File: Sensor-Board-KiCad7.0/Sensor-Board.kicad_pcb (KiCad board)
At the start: 2 copper layers, 61 x 22.9 mm, 128 parts, among them J1 B4B-XH-A, U1 OPA396DCKT, U10 BME680, U11 OPA396DCKT, U12 OPA396DCKT, U13 TCA9548AMRGER, U14 OPA396DCKT, U15 MMBFJ177LT1, U16 MMBFJ177LT1, U17 MMBFJ177LT1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

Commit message: Added gas cell contour and Echem sensors
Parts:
- moved U10 234.4 mm to (121.8, 95.7), turned to -90 degrees
- moved U27 148.2 mm to (131.3, 91.7)
- moved U28 143.0 mm to (138.2, 84.2), turned to -90 degrees
- moved U23 139.1 mm to (144.1, 98.9), turned to 180 degrees
- moved U6 129.5 mm to (153.8, 95.5)
- moved U29 121.8 mm to (137.1, 96.8), turned to 90 degrees
- moved U30 121.2 mm to (137.0, 106.9), turned to 90 degrees
- moved U31 118.4 mm to (138.2, 94.3), turned to -90 degrees
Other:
- board size 61 x 22.9 mm -> 188.3 x 126.4 mm

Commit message: Clarified exclusion zones and started layout
Clarified the zones where we cannot place components and started adding components to layout.
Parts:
- moved U3 260.2 mm to (123.1, 130.9), turned to 90 degrees
- moved U2 260.1 mm to (123.2, 126.9), turned to 90 degrees
- moved U1 260.0 mm to (123.2, 122.5), turned to 90 degrees
- moved U26 247.0 mm to (133.5, 122.5), turned to -90 degrees
- moved R55 242.9 mm to (120.8, 124.8), turned to -90 degrees
- moved U20 242.7 mm to (133.5, 131.2), turned to -90 degrees
- moved U19 237.8 mm to (133.5, 127.0), turned to -90 degrees
- moved R56 236.3 mm to (126.5, 124.0), turned to 180 degrees
- moved R4 232.6 mm to (120.8, 131.2), turned to 90 degrees
- moved R57 231.5 mm to (129.8, 122.2), turned to 180 degrees
- moved R2 228.4 mm to (126.5, 128.2), turned to 180 degrees
- moved R5 226.7 mm to (126.6, 132.2), turned to 180 degrees
- moved C2 224.7 mm to (126.5, 130.5), turned to 180 degrees
- moved C1 224.0 mm to (126.5, 126.5), turned to 180 degrees
- moved R3 223.6 mm to (129.7, 126.5), turned to 180 degrees
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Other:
- outline, holes or cut-outs redrawn

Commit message: layout of pcb update (not final)
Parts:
- moved TP15 280.8 mm to (107.2, 111.8)
- moved TP14 279.1 mm to (109.9, 111.8)
- moved TP13 278.8 mm to (101.3, 102.1)
- moved R21 246.3 mm to (105.5, 116.7), turned to 45 degrees
- moved R22 242.4 mm to (107.8, 114.4), turned to -135 degrees
- moved TP16 239.1 mm to (156.1, 131.9)
- moved U21 239.0 mm to (142.5, 127.3), turned to 90 degrees
- moved U22 239.0 mm to (142.5, 131.4), turned to 90 degrees
- moved U14 238.8 mm to (142.5, 122.5), turned to 90 degrees
- moved C4 236.2 mm to (101.3, 105.2), turned to 90 degrees
- moved TP17 234.6 mm to (157.8, 127.0)
- moved TP18 232.6 mm to (159.4, 129.3)
- moved R67 226.2 mm to (139.2, 132.1), turned to 180 degrees
- moved U25 223.9 mm to (108.2, 106.4), turned to -90 degrees
- moved R69 223.3 mm to (139.2, 130.5), turned to 180 degrees
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
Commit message: Full preliminary layout
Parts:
- moved TP1 274.5 mm to (104.5, 79.8)
- moved TP2 273.7 mm to (104.5, 77.2)
- moved C9 235.1 mm to (101.0, 105.7), turned to 90 degrees
- moved C8 234.9 mm to (101.0, 102.6), turned to -90 degrees
- moved R20 227.1 mm to (104.5, 75.0), turned to 180 degrees
- moved R19 222.7 mm to (110.1, 80.2)
- moved R68 220.4 mm to (144.4, 132.2)
- moved R53 210.8 mm to (144.4, 128.2)
- moved R7 205.0 mm to (144.4, 124.2)
- moved R29 180.9 mm to (166.6, 113.2), turned to -45 degrees
- moved R16 133.6 mm to (101.0, 111.9), turned to -90 degrees
- moved C6 127.8 mm to (101.0, 89.0), turned to 90 degrees
- moved C5 127.7 mm to (101.0, 85.8), turned to -90 degrees
- moved C15 126.5 mm to (101.0, 82.6), turned to 90 degrees
- moved R17 124.3 mm to (110.0, 111.3), turned to 180 degrees
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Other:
- outline, holes or cut-outs redrawn

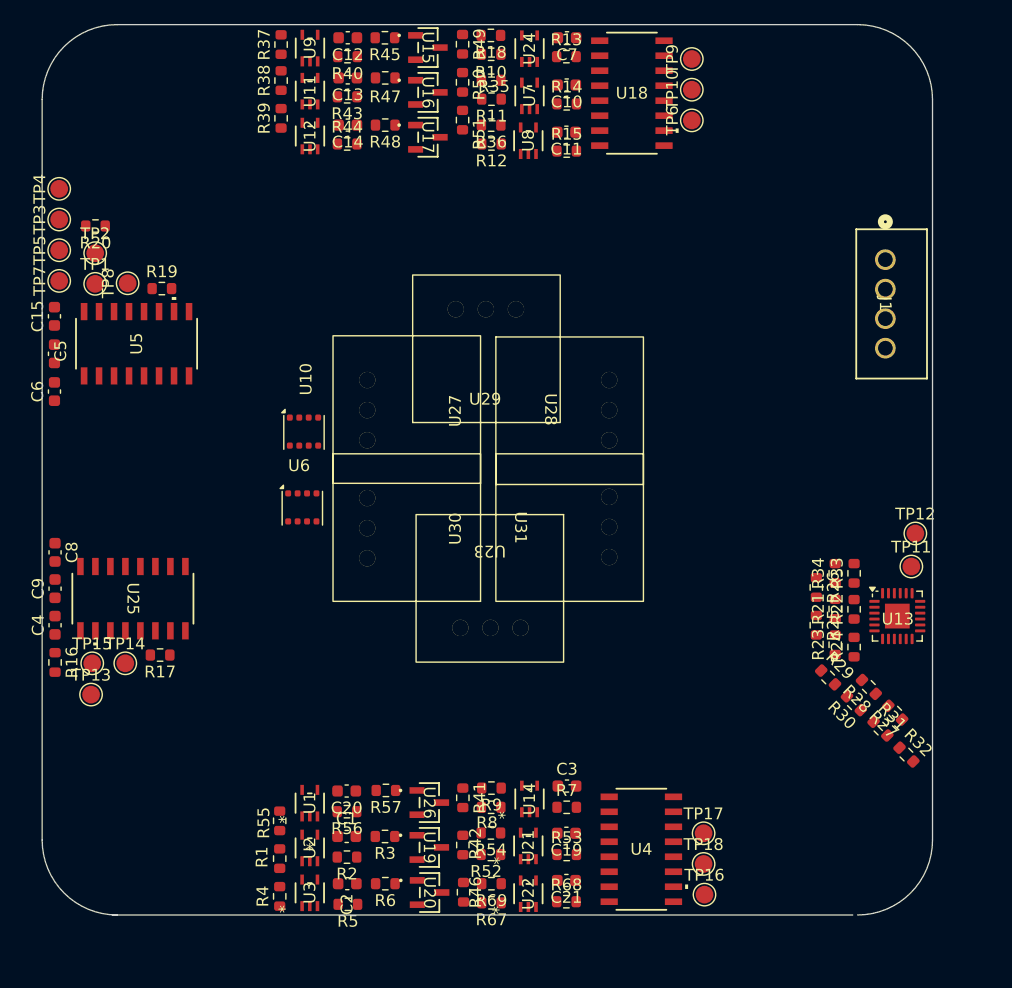
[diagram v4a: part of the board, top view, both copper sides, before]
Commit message: Fixed board dimensions
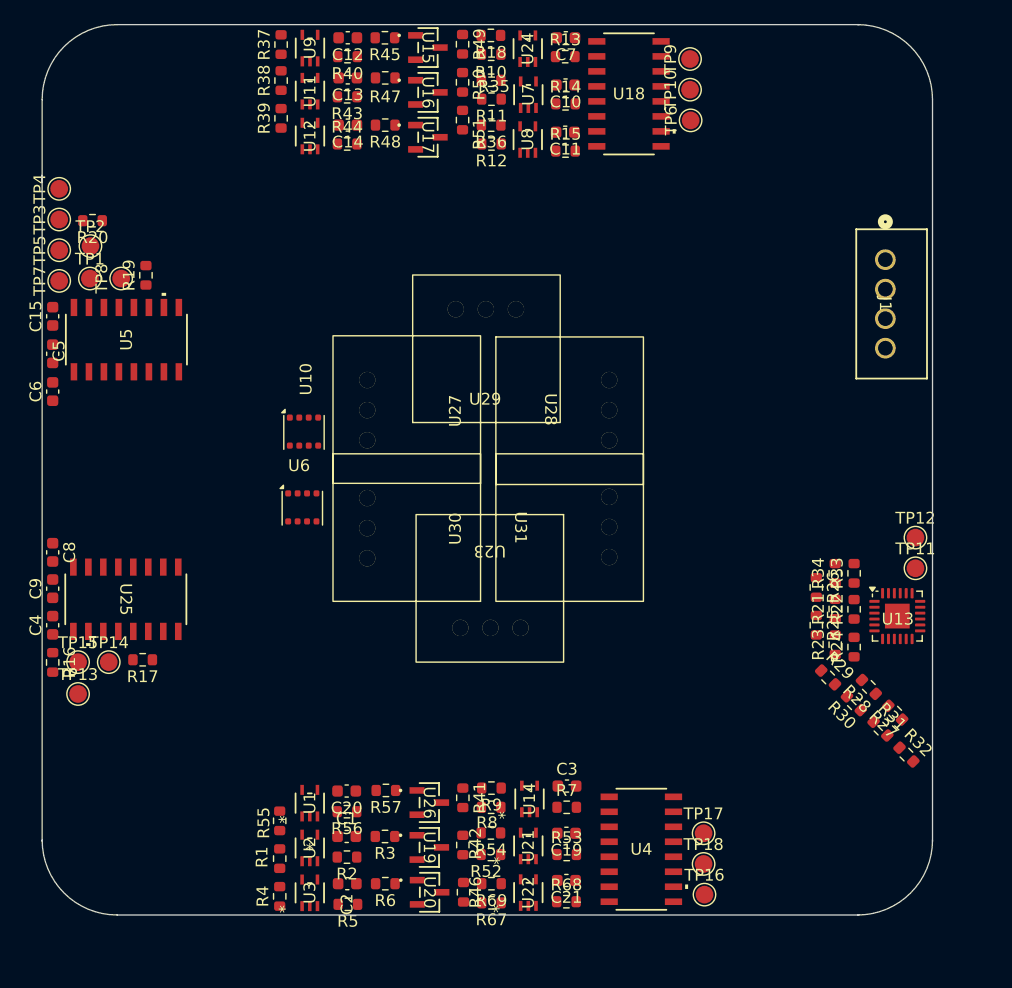
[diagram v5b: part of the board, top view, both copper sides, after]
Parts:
- moved R19 1.76 mm to (108.8, 79.1), turned to 90 degrees
- moved R17 1.53 mm to (108.5, 111.7)
- moved TP14 1.40 mm to (105.6, 111.9)
- moved TP15 1.20 mm to (103.0, 111.9)
- moved TP13 1.10 mm to (103.0, 114.6)
- moved U5 0.93 mm to (107.1, 84.6)
- moved TP2 0.72 mm to (104.0, 76.7)
- moved TP8 0.68 mm to (106.7, 79.4)
- moved TP1 0.64 mm to (104.0, 79.4)
- moved U25 0.60 mm to (107.0, 106.6)
- moved R20 0.51 mm to (104.2, 74.5)
- moved TP11 0.38 mm to (173.9, 104.0)
- moved TP12 0.35 mm to (173.9, 101.3)
- moved U18 0.26 mm to (149.7, 63.8)
- moved C4 0.20 mm to (100.8, 108.8)
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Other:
- outline, holes or cut-outs redrawn

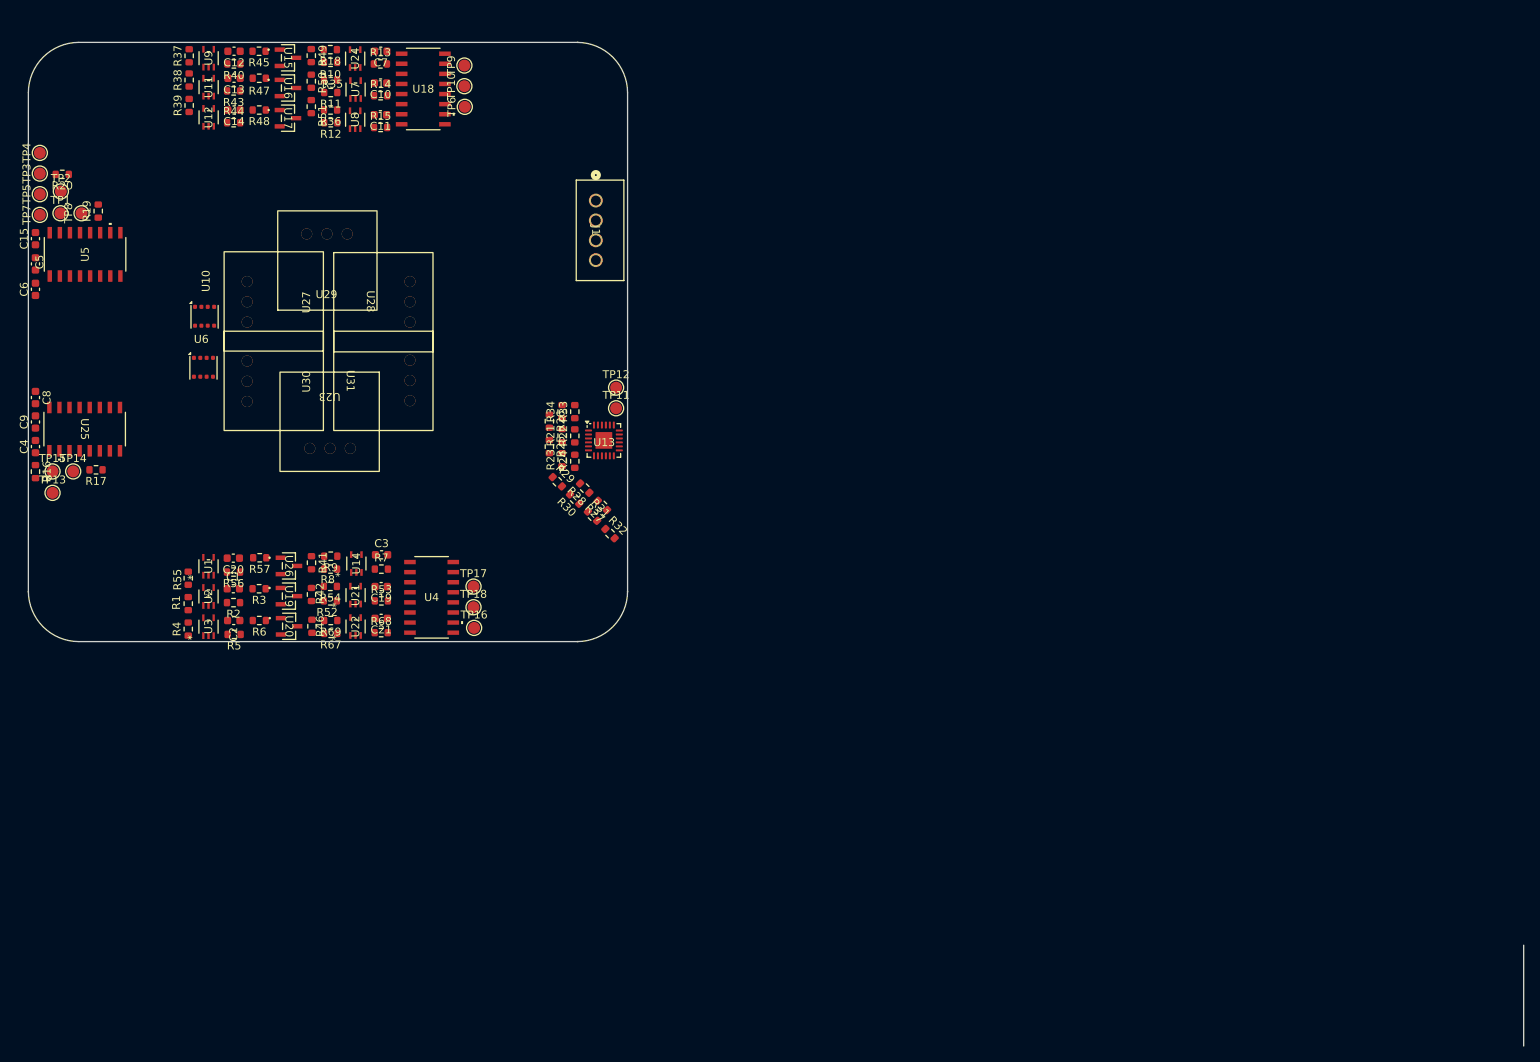
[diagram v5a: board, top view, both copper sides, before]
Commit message: Started routing traces in layout
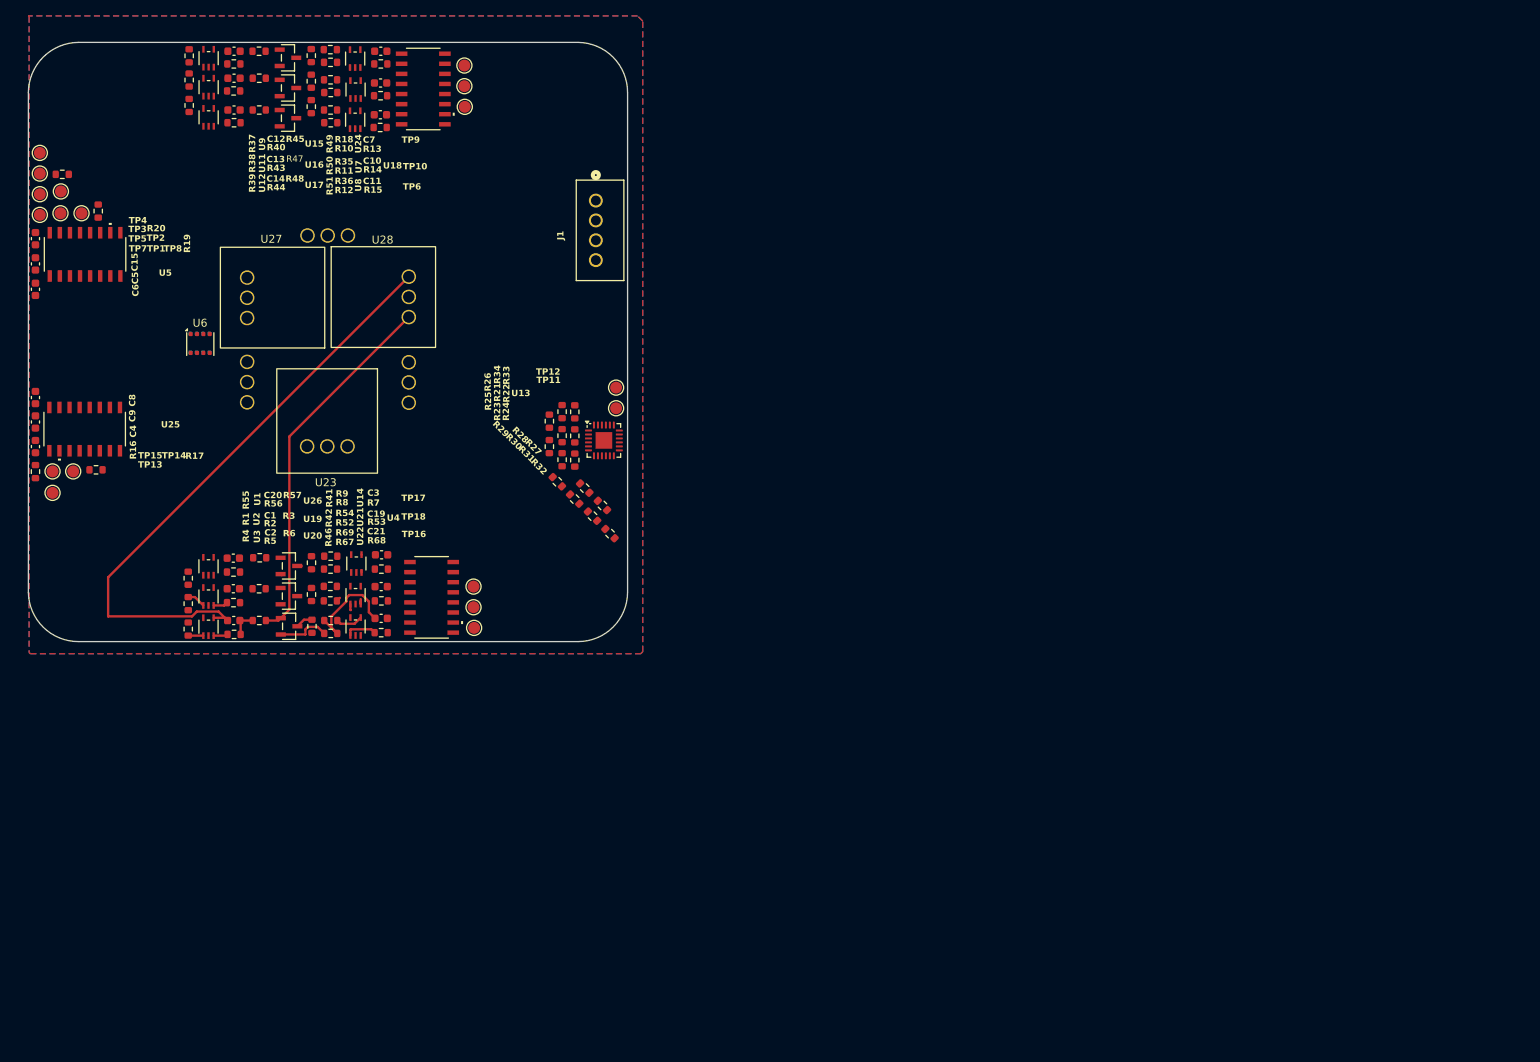
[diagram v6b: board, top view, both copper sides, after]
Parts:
- U10, U29, U30, U31: moved to B.Cu
- moved U29 12.7 mm to (143.9, 91.9), turned to 180 degrees
- moved U10 3.43 mm to (121.5, 95.8), turned to 180 degrees
- moved U6 3.02 mm to (121.6, 95.8)
- moved U31 1.12 mm to (137.2, 94.4)
- moved U30 0.96 mm to (138.2, 107.0)
- moved U28 0.62 mm to (138.2, 83.7)
- moved U27 0.53 mm to (137.2, 96.3)
- moved U23 0.44 mm to (143.9, 99.0)
- moved R24 0.15 mm to (168.8, 110.5)
- moved R15 0.05 mm to (144.2, 68.6)
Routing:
- net Count1_SO2: track 0.00 -> 76.1 mm
- net Ref1_SO2: track 0.00 -> 46.6 mm
- net Net-(U22--IN): track 0.00 -> 13.6 mm
- net Sens1_SO2: track 0.00 -> 6.57 mm
- net Net-(U22-+IN): track 0.00 -> 3.97 mm
- net AOut1_SO2: track 0.00 -> 3.44 mm
- net Net-(C2-Pad1): track 0.00 -> 3.42 mm
- net Net-(U2-+IN): track 0.00 -> 2.33 mm
- net Net-(U20-G): track 0.00 -> 2.18 mm
- net Net-(U3-+IN): track 0.00 -> 1.90 mm
- net Net-(U2--IN): track 0.00 -> 1.82 mm
- net Net-(U3--IN): track 0.00 -> 1.81 mm
- net Net-(U21--IN): track 0.00 -> 1.74 mm
- net Net-(U21-+IN): track 0.00 -> 0.80 mm
- net Net-(U26-G): track 0.00 -> 0.57 mm
- added copper zone on B.Cu, net GND
- added copper zone on F.Cu, net GND
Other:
- board size 188.3 x 126.4 mm -> 75.4 x 75.4 mm

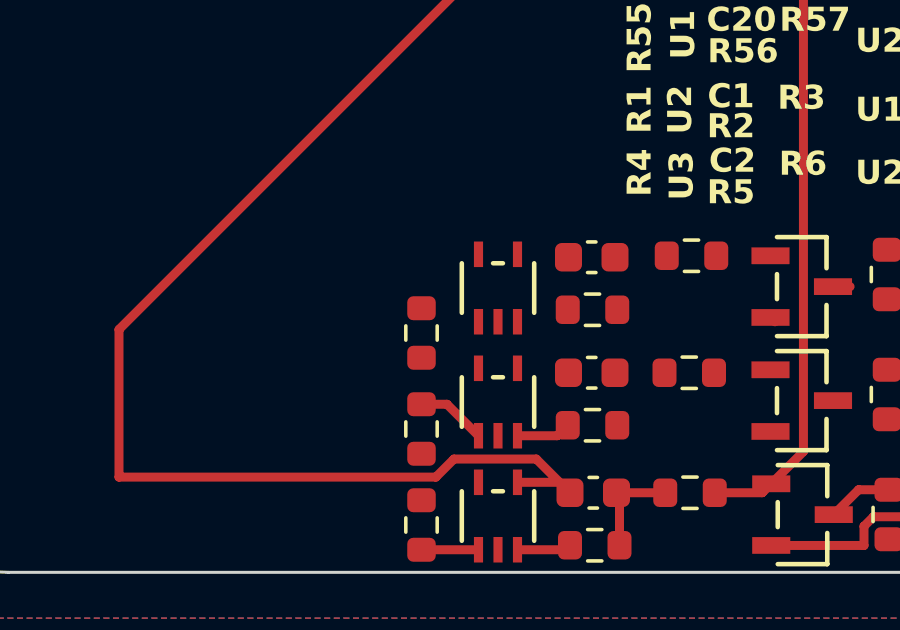
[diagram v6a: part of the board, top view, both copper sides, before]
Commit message: Changed silkscreen size and location
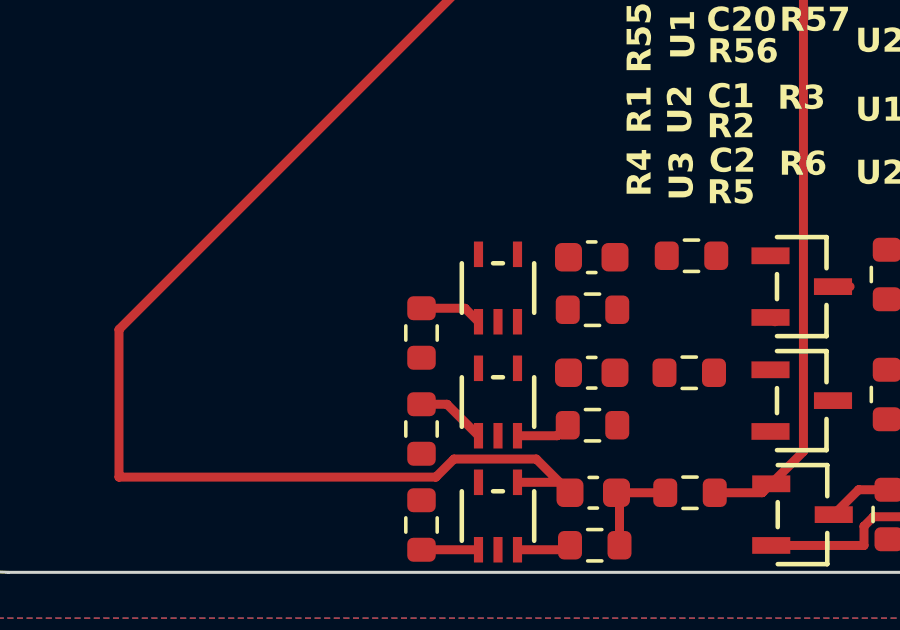
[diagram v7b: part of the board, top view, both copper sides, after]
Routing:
- net Net-(U1-+IN): track 0.00 -> 2.09 mm
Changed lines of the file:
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@@
   (segment (start 140.500015 128.5963) (end 140.500015 129.32175) (width 0.3) (layer "F.Cu") (net 89))
   (segment (start 140.500015 129.32175) (end 140.550015 129.37175) (width 0.3) (layer "F.Cu") (net 89))
+  (segment (start 121.533628 124.5213) (end 121.983628 124.9713) (width 0.3) (layer "F.Cu") (net 90))
+  (segment (start 120.0836 124.5213) (end 121.533628 124.5213) (width 0.3) (layer "F.Cu") (net 90))
   (segment (start 135.150242 131.4713) (end 136.375 131.4713) (width 0.3) (layer "F.Cu") (net 93))
   (segment (start 134.8336 132.4287) (end 134.8336 131.787942) (width 0.3) (layer "F.Cu") (net 93))
